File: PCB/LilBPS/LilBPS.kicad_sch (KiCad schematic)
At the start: 45 parts, among them J1 Screw_Terminal_01x02, J2 Conn_01x02_Pin, J3 USB_C_Receptacle_PowerOnly_6P, P1 USB_C_Plug_USB2.0, Q1 DMP3013SFV, Q2 DMP3013SFV, SW1 SW_Push, SW2 SW_Push, U1 STUSB4500QTR, U2 AMS1117-3.3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

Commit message: First journal entry :D
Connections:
- net Vsnk: now reaches C11.1, D3.C, J1.1 (Pin_1), Q2.1 (S), Q2.2 (S), Q2.3 (S)
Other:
- note added: "MCU Circuit"
- note added: "MCU USB C Port"
- note added: "USB C PD Handling"
- note added: "USB C PD Port"
- note removed: "MCU USB"
- note removed: "USB C PD"
- note removed: "USB C PD Controller"
- moved on the sheet: C1, C2, D1, D2, D3, D4, D6, J1, J2, J3, P1, Q1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

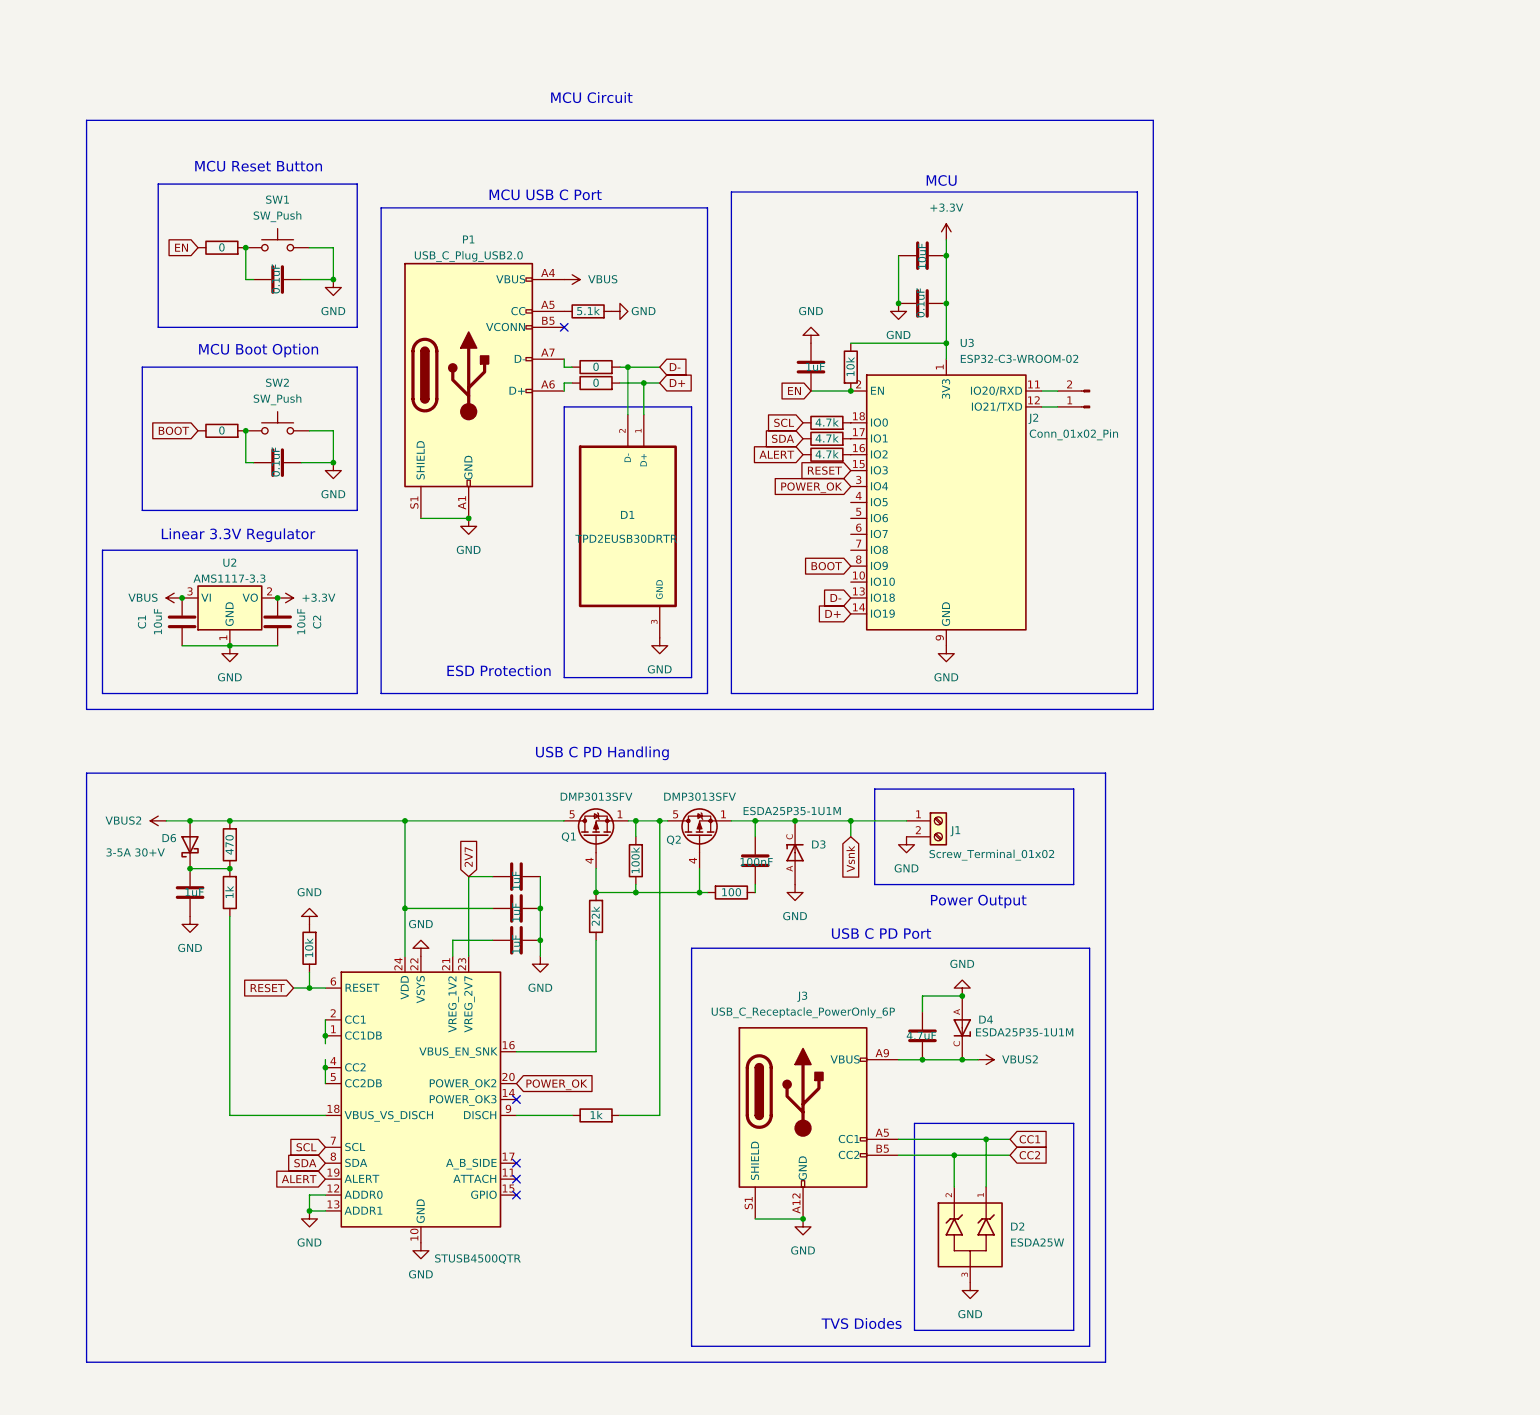
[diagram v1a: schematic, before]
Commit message: Fix stuff i messed up when moving the schematic
also decrease the hours for yesterday, think it was closer to 3
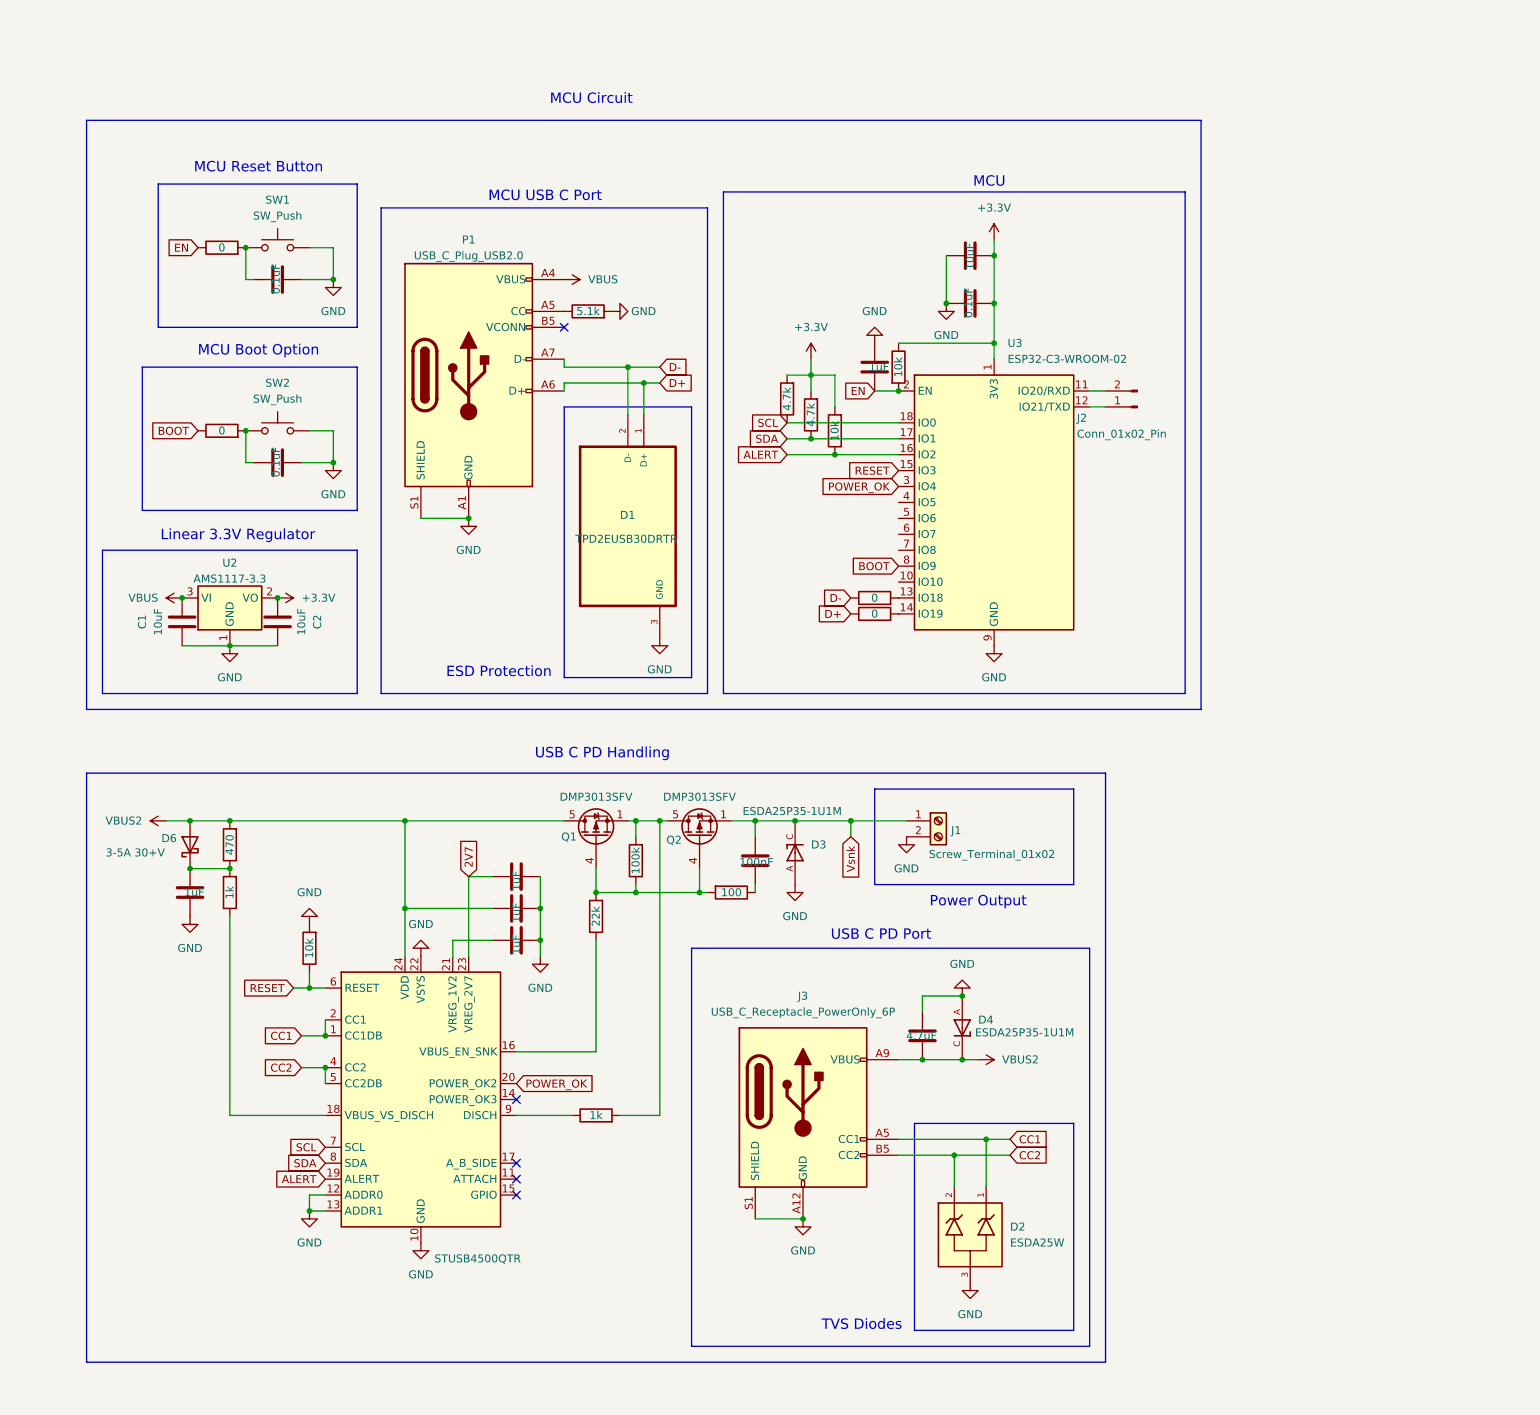
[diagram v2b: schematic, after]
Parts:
- R9: value 4.7k -> 10k
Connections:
- net +3.3V: now also R7.2, R8.2, R9.2
- net ALERT: now also U3.16 (IO2)
- net CC1: now also U1.1 (CC1DB), U1.2 (CC1)
- net CC2: now also U1.4 (CC2), U1.5 (CC2DB)
- net D+: now also P1.A6 (D+), R1.1; no longer R1.2, U3.14 (IO19)
- net D-: now also P1.A7 (D-), R2.1; no longer R2.2, U3.13 (IO18)
- net SCL: now also U3.18 (IO0)
- net SDA: now also U3.17 (IO1)
- new net: R1.2, U3.14 (IO19)
- new net: R2.2, U3.13 (IO18)
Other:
- moved on the sheet: J2, U3
